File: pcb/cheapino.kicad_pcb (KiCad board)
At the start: 2 copper layers, 132.5 x 95.1 mm, 65 parts, among them K1 SW_Push, K10 SW_Push, K11 SW_Push, K12 SW_Push, K13 SW_Push, K14 SW_Push, K15 SW_Push, K16 SW_Push, K17 SW_Push, K18 SW_Push, K19 K19, K2 SW_Push, K20 K20, K21 K21, K3 SW_Push, K4 SW_Push, K5 SW_Push, K6 SW_Push, K7 SW_Push, K8 SW_Push, K9 SW_Push, U1 RP2040-Zero

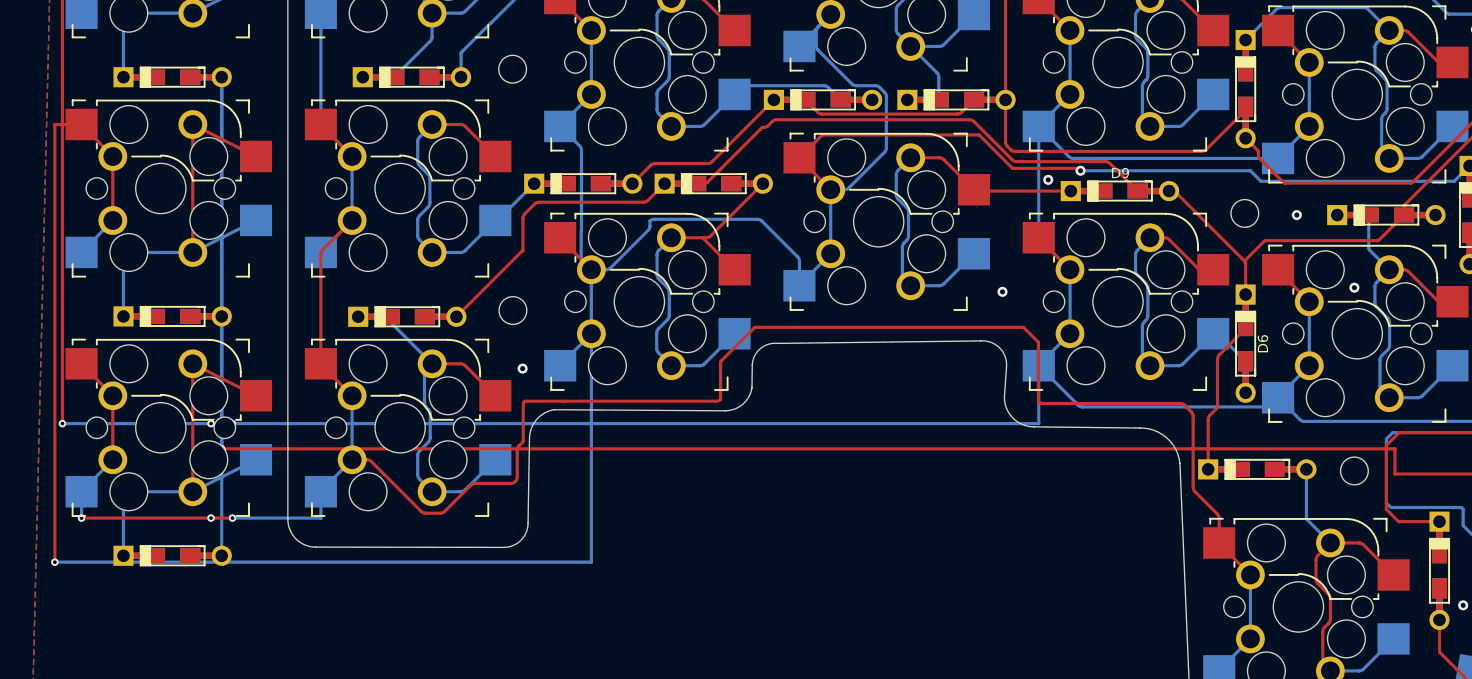
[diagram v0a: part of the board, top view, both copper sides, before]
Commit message: Finish 6-column routing: resolve the 2 remaining DRC shorts
- Move ROW_4 long F.Cu horizontal from y=110.0 → y=109.5 (clears COL_3 F.Cu vertical near x=78.3)
- Move COL_2 B.Cu horizontal from y=119.0 → y=122.0 (clears D24 diode pads at y≈118.5)
- Update connecting vias and stubs accordingly
- Mark SIX_COLUMN_HANDOFF.md as finished

Board should now have 0 new shorts (baseline 3 unconnected GND artifacts remain).
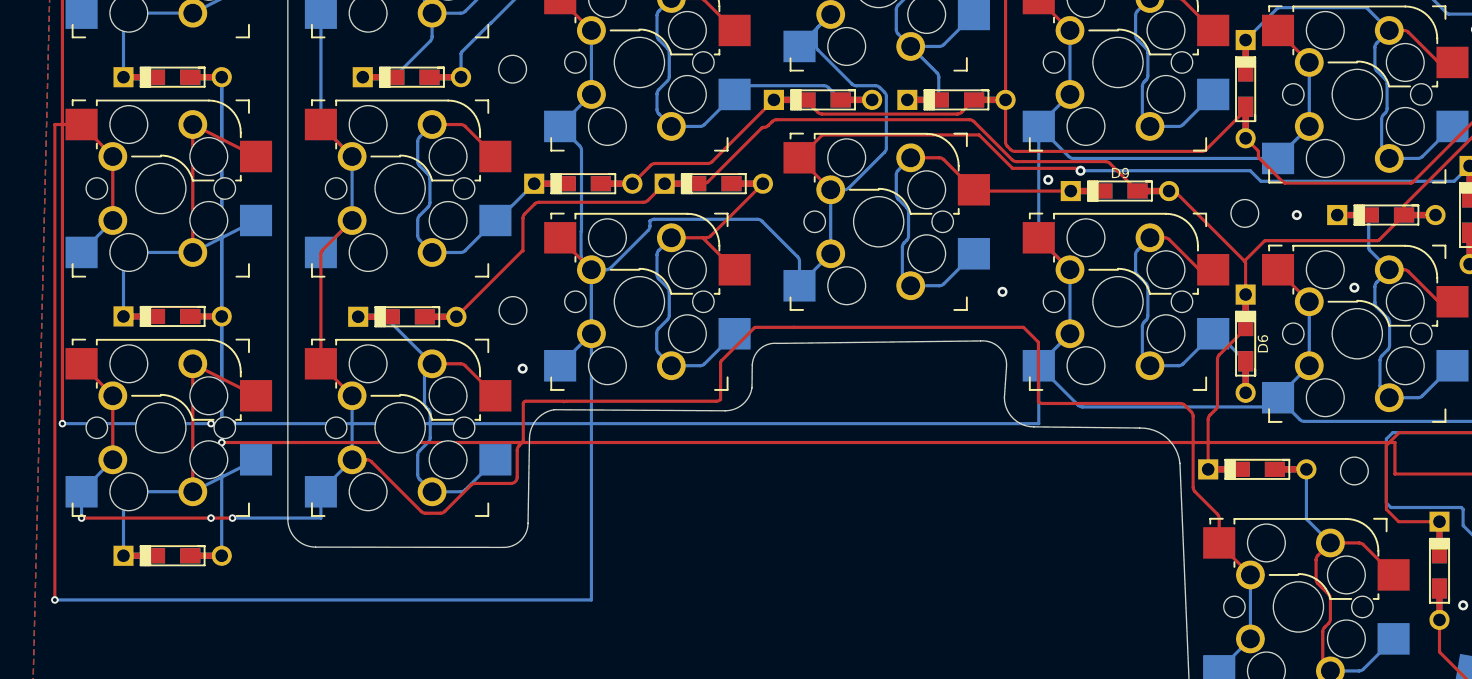
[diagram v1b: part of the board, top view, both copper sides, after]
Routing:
- net COL_2: track 376.5 -> 382.5 mm
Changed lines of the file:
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@@
 	(segment
 		(start 41.6 84.25)
-		(end 41.6 119.0)
+		(end 41.6 122.0)
 		(width 0.25)
 		(layer "F.Cu")
@@
 	)
 	(segment
-		(start 41.6 119.0)
-		(end 84.2 119.0)
+		(start 41.6 122.0)
+		(end 84.2 122.0)
 		(width 0.25)
 		(layer "B.Cu")
@@
 	)
 	(segment
-		(start 84.2 119.0)
+		(start 84.2 122.0)
 		(end 84.2 95.8)
 		(width 0.25)
@@
 	(segment
 		(start 54.85 80.49)
-		(end 54.85 110.0)
+		(end 54.85 109.5)
 		(width 0.25)
 		(layer "B.Cu")
@@
 	)
 	(segment
-		(start 54.85 110.0)
-		(end 148.0 110.0)
+		(start 54.85 109.5)
+		(end 148.0 109.5)
 		(width 0.25)
 		(layer "F.Cu")
@@
 	)
 	(segment
-		(start 148.0 110.0)
+		(start 148.0 109.5)
 		(end 148.0 112.0)
 		(width 0.25)
@@
 	)
 	(via
-		(at 41.6 119.0)
+		(at 41.6 122.0)
 		(size 0.6)
 		(drill 0.3)
@@
 	)
 	(via
-		(at 54.85 110.0)
+		(at 54.85 109.5)
 		(size 0.6)
 		(drill 0.3)

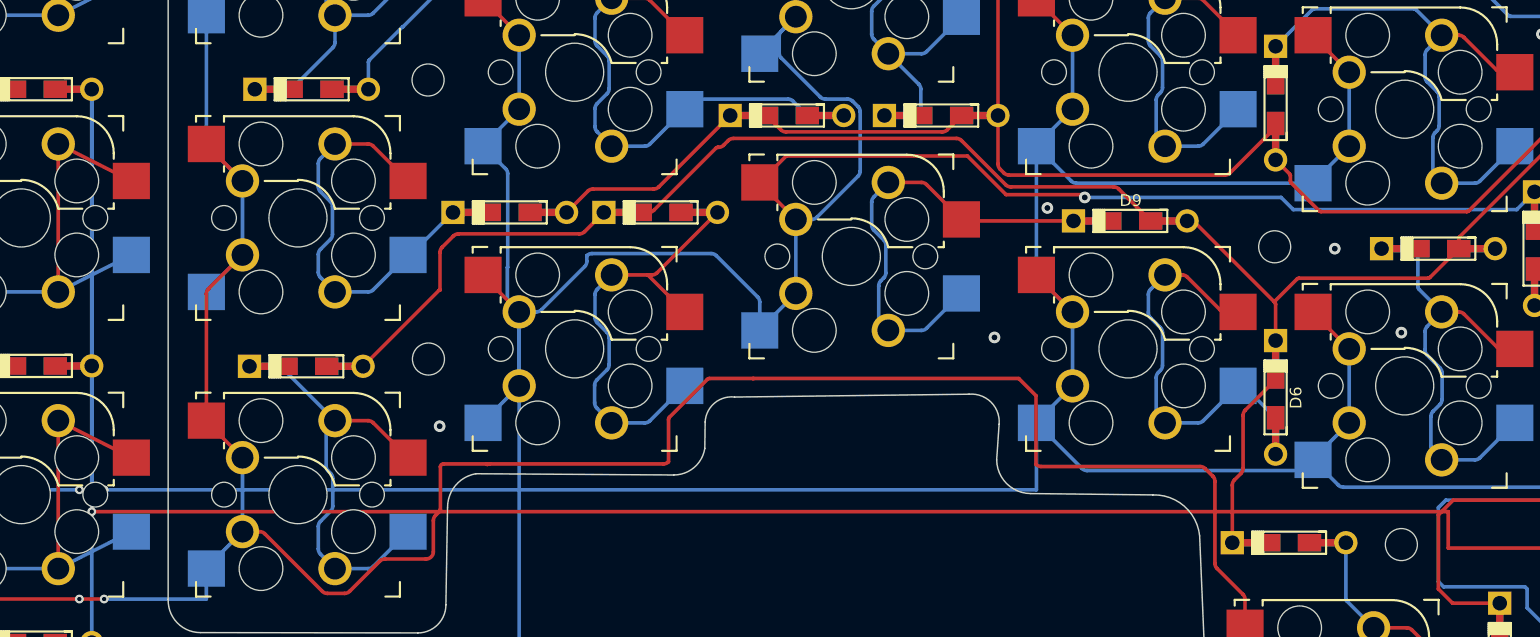
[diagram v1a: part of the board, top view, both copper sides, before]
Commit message: Fix remaining DRC shorts: ROW_4 long run on B.Cu at y=111 (0 shorts with KiCad 8.0.9)
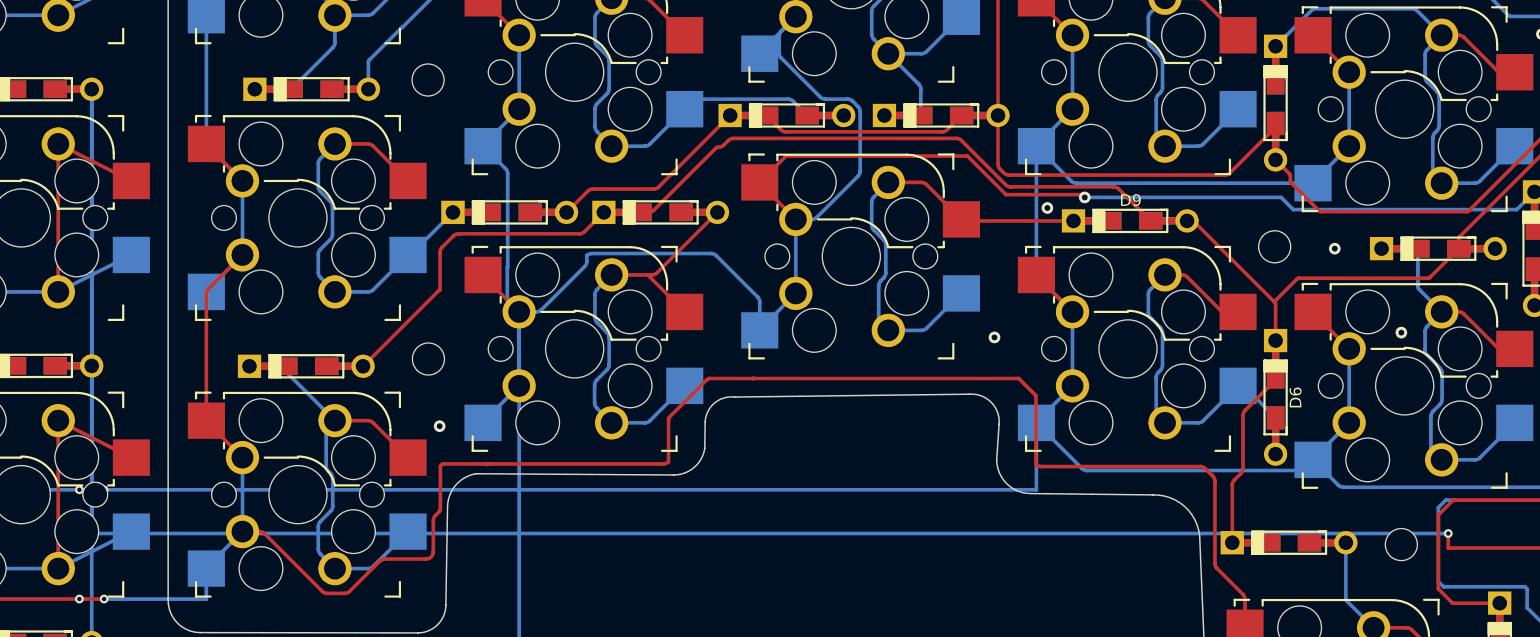
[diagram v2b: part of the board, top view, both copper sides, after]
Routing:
- net ROW_4: vias 3 -> 4
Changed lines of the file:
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@@
 	(segment
 		(start 54.85 80.49)
-		(end 54.85 109.5)
+		(end 54.85 111.0)
 		(width 0.25)
 		(layer "B.Cu")
@@
 	)
 	(segment
-		(start 54.85 109.5)
-		(end 148.0 109.5)
+		(start 54.85 111.0)
+		(end 148.0 111.0)
 		(width 0.25)
-		(layer "F.Cu")
+		(layer "B.Cu")
 		(net 28)
 	)
 	(segment
-		(start 148.0 109.5)
+		(start 148.0 111.0)
 		(end 148.0 112.0)
 		(width 0.25)
@@
 		(width 0.25)
 		(layer "F.Cu")
+		(net 28)
+	)
+	(via
+		(at 148.0 111.0)
+		(size 0.6)
+		(drill 0.3)
+		(layers "F.Cu" "B.Cu")
 		(net 28)
 	)
@@
 	)
 	(via
-		(at 54.85 109.5)
+		(at 54.85 111.0)
 		(size 0.6)
 		(drill 0.3)

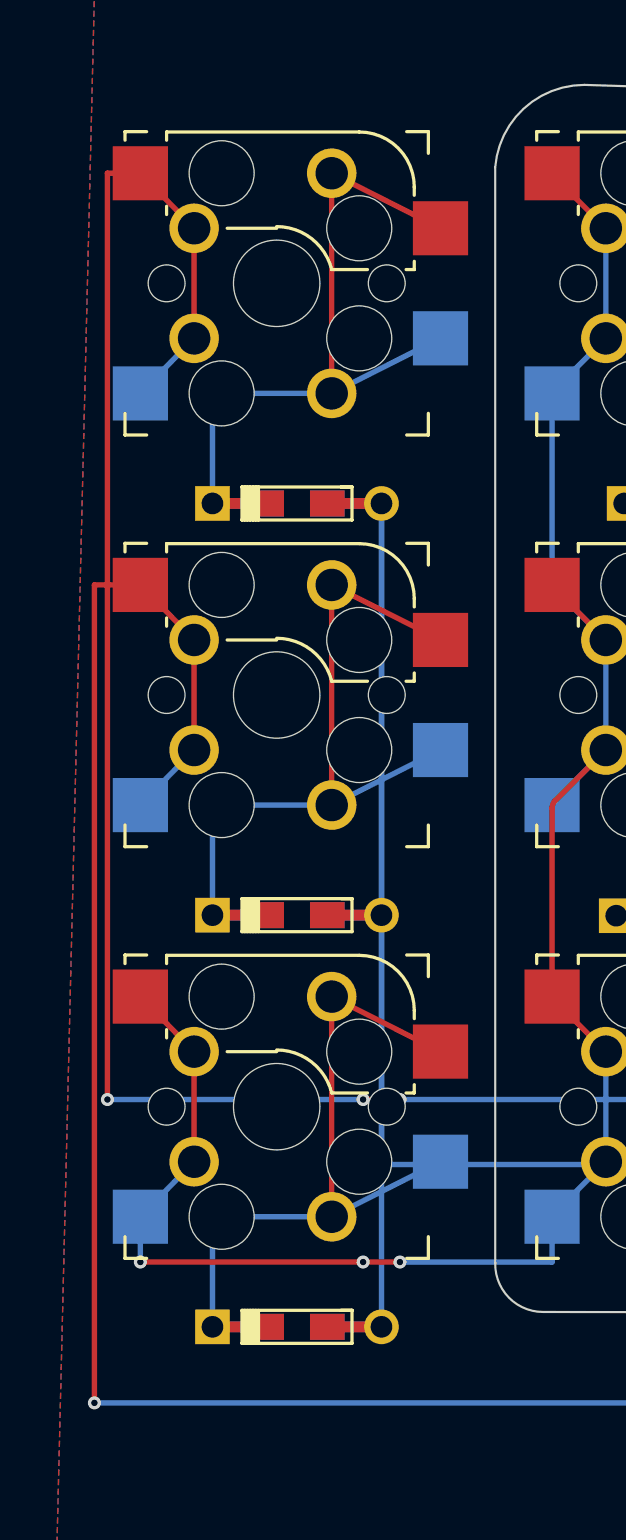
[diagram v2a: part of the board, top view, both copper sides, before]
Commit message: Shift new column down 3mm and extend left outline to enclose keys
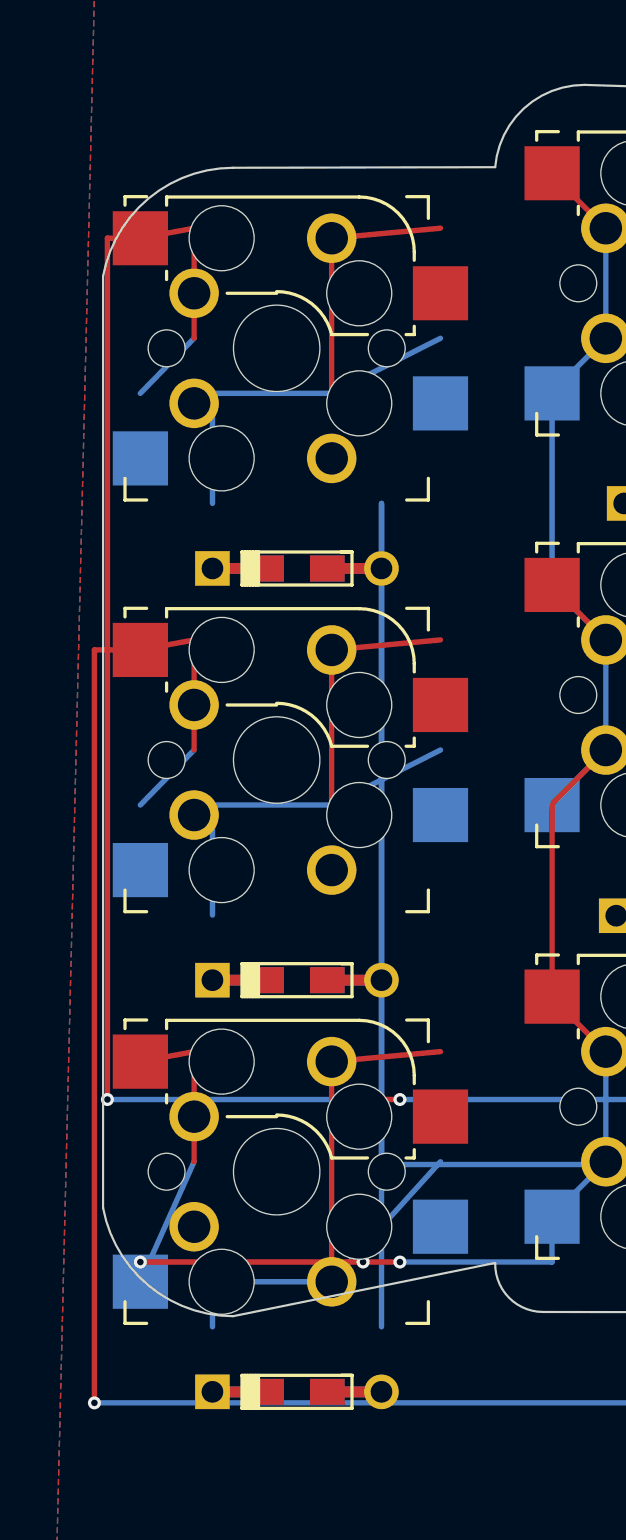
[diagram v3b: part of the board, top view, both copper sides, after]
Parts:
- moved D22 3.00 mm to (50.9, 83.5)
- moved D23 3.00 mm to (50.9, 102.5)
- moved D24 3.00 mm to (50.9, 121.5)
- moved K19 3.00 mm to (50.0, 73.3)
- moved K20 3.00 mm to (50.0, 92.3)
- moved K21 3.00 mm to (50.0, 111.3)
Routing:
- net COL_2: track 382.5 -> 378.5 mm
- net COL_1: track 367.7 -> 363.7 mm
- net Net-(D23-K): track 32.0 -> 28.4 mm
- net Net-(D22-K): track 32.0 -> 28.4 mm
- net Net-(D24-K): track 32.0 -> 30.3 mm
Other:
- board size 132.5 x 95.1 mm -> 150.6 x 95.1 mm
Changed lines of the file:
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@@
 		(footprint "project_footprints:Kailh_socket_MX_optional_reversible"
 		(layer "F.Cu")
-		(at 50.0118 70.3326)
+		(at 50.0118 73.3326)
 		(descr "MX-style keyswitch with support for reversible optional Kailh socket")
 		(tags "MX,cherry,gateron,kailh,pg1511,socket")
@@
 	(footprint "project_footprints:Kailh_socket_MX_optional_reversible"
 		(layer "F.Cu")
-		(at 50.0118 89.3318)
+		(at 50.0118 92.3318)
 		(descr "MX-style keyswitch with support for reversible optional Kailh socket")
 		(tags "MX,cherry,gateron,kailh,pg1511,socket")
@@
 	(footprint "project_footprints:Kailh_socket_MX_optional_reversible"
 		(layer "F.Cu")
-		(at 50.0118 108.3310)
+		(at 50.0118 111.3310)
 		(descr "MX-style keyswitch with support for reversible optional Kailh socket")
 		(tags "MX,cherry,gateron,kailh,pg1511,socket")
@@
 	(footprint "keebio:Diode-dual"
 		(layer "F.Cu")
-		(at 50.9486 80.4926 180)
+		(at 50.9486 83.4926 180)
 		(property "Reference" "D22"
 			(at -0.0254 1.4 0)
@@
 	(footprint "keebio:Diode-dual"
 		(layer "F.Cu")
-		(at 50.9486 99.4918 180)
+		(at 50.9486 102.4918 180)
 		(property "Reference" "D23"
 			(at -0.0254 1.4 0)
@@
 	(footprint "keebio:Diode-dual"
 		(layer "F.Cu")
-		(at 50.9486 118.4910 180)
+		(at 50.9486 121.4910 180)
 		(property "Reference" "D24"
 			(at -0.0254 1.4 0)
@@
 	(gr_line
 		(start 60.097766 115.541608)
+		(end 48.0 118.0)
+		(stroke
+			(width 0.1)
+			(type solid)
+		)
+		(layer "Edge.Cuts")
+	)
+	(gr_arc
+		(start 48.0 118.0)
+		(mid 44.0 116.5)
+		(end 42.0 113.0)
+		(stroke
+			(width 0.1)
+			(type solid)
+		)
+		(layer "Edge.Cuts")
+	)
+	(gr_line
+		(start 42.0 113.0)
+		(end 42.0 70.0)
+		(stroke
+			(width 0.1)
+			(type solid)
+		)
+		(layer "Edge.Cuts")
+	)
+	(gr_arc
+		(start 42.0 70.0)
+		(mid 44.0 66.5)
+		(end 48.0 65.0)
+		(stroke
+			(width 0.1)
+			(type solid)
+		)
+		(layer "Edge.Cuts")
+	)
+	(gr_line
+		(start 48.0 65.0)
+		(end 60.096401 64.9732)
+		(stroke
+			(width 0.1)
+			(type solid)
+		)
+		(layer "Edge.Cuts")
+	)
+(gr_line
+		(start 60.097766 115.541608)
 		(end 60.096401 64.9732)
 		(stroke
@@
 			(type solid)
 		)
+		(layer "Dwgs.User")
+		(stroke
+			(width 0.1)
+			(type solid)
+		)
 		(layer "Edge.Cuts")
 	)
@@
 	)
 	(segment
-		(start 43.72 65.25)
+		(start 43.72 68.2500)
 		(end 46.2 67.79)
 		(width 0.25)
@@
 	)
 	(segment
-		(start 43.72 84.25)
+		(start 43.72 87.2500)
 		(end 46.2 86.79)
 		(width 0.25)
@@
 	)
 	(segment
-		(start 43.72 103.25)
+		(start 43.72 106.2500)
 		(end 46.2 105.79)
 		(width 0.25)
@@
 	(segment
 		(start 46.2 110.87)
-		(end 43.72 113.41)
+		(end 43.72 116.4100)
 		(width 0.25)
 		(layer "B.Cu")
@@
 	)
 	(segment
-		(start 52.55 65.25)
+		(start 52.55 68.2500)
 		(end 57.57 67.79)
 		(width 0.25)
@@
 	)
 	(segment
-		(start 52.55 65.25)
+		(start 52.55 68.2500)
 		(end 52.55 75.41)
 		(width 0.25)
@@
 	)
 	(segment
-		(start 52.55 84.25)
+		(start 52.55 87.2500)
 		(end 57.57 86.79)
 		(width 0.25)
@@
 	)
 	(segment
-		(start 52.55 84.25)
+		(start 52.55 87.2500)
 		(end 52.55 94.41)
 		(width 0.25)
@@
 	)
 	(segment
-		(start 52.55 103.25)
+		(start 52.55 106.2500)
 		(end 57.57 105.79)
 		(width 0.25)
@@
 	)
 	(segment
-		(start 52.55 103.25)
-		(end 52.55 113.41)
+		(start 52.55 106.2500)
+		(end 52.55 116.4100)
 		(width 0.25)
 		(layer "F.Cu")
@@
 	(segment
 		(start 57.57 110.87)
-		(end 52.55 113.41)
+		(end 52.55 116.4100)
 		(width 0.25)
 		(layer "B.Cu")
@@
 	)
 	(segment
-		(start 43.72 113.41)
+		(start 43.72 116.4100)
 		(end 43.72 115.5)
 		(width 0.25)
@@
 	)
 	(segment
-		(start 43.72 84.25)
-		(end 41.6 84.25)
+		(start 43.72 87.2500)
+		(end 41.6 87.2500)
 		(width 0.25)
 		(layer "F.Cu")
@@
 	)
 	(segment
-		(start 41.6 84.25)
+		(start 41.6 87.2500)
 		(end 41.6 122.0)
 		(width 0.25)
@@
 	)
 	(segment
-		(start 43.72 65.25)
-		(end 42.2 65.25)
+		(start 43.72 68.2500)
+		(end 42.2 68.2500)
 		(width 0.25)
 		(layer "F.Cu")
@@
 	)
 	(segment
-		(start 42.2 65.25)
+		(start 42.2 68.2500)
 		(end 42.2 108.0)
 		(width 0.25)
@@
 	)
 	(segment
-		(start 52.55 113.41)
-		(end 47.05 113.41)
+		(start 52.55 116.4100)
+		(end 47.05 116.4100)
 		(width 0.25)
 		(layer "B.Cu")
@@
 	)
 	(segment
-		(start 47.05 113.41)
+		(start 47.05 116.4100)
 		(end 47.05 118.49)
 		(width 0.25)
